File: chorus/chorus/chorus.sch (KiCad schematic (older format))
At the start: 39 parts

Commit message: working digital clock
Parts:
- removed C?: 220p, symbol Device:C
- removed C?: C, symbol Device:C
- removed R?: 3.8K, symbol Device:R
- removed RV?: 68K, symbol Device:R_POT
- added C? (x2): 10u, symbol Device:CP1
- added D? (x4): D, symbol Device:D
- added Q? (x2): 2N3906, Package_TO_SOT_THT:TO-92_Inline, symbol Transistor_BJT:2N3906
- added R? (x2): 2.8k, symbol Device:R
- added R?: 1K, symbol Device:R
- added R? (x2): 2.2k, symbol Device:R
- added R?: 10k, symbol Device:R
- added R?: 4.7k, symbol Device:R
- added RV?: 10K, symbol Device:R_POT
- added U? (x2): TL074, symbol Amplifier_Operational:TL074
- added U?: LM13700, symbol Amplifier_Operational:LM13700
- R?: value R -> 82K
- R?: value R -> 330K
- R?: value R -> 20K
- RV?: value R -> 500K
- U?: value MN3207 -> TL074
- U?: value MN3102 -> TL074
- U?: value ATtiny85-20PU -> TL074; footprint Package_DIP:DIP-8_W7.62mm -> (none)
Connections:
- net GND: now also U?.2 (-), U?.5 (+), D?.1 (K), D?.2 (A), Q?.1 (E), Q?.1 (E), R?.2, U?.12 (+); no longer U?.10 (+), U?.13 (-)
- net at R?.1: now also U?.7, C?.1, D?.1 (K), D?.2 (A); no longer U?.8
- net at RV?.3: now also U?.6 (-), C?.1; no longer U?.9 (-)
- net at R?.2, R?.2: now also U?.3 (+); no longer U?.12 (+)
- net at R?.1, R?.2: now also U?.1; no longer U?.14
- new net: C?.2, C?.2
- new net: D?.2 (A), D?.2 (A), R?.2
- new net: D?.1 (K), D?.1 (K), R?.2
- new net: R?.1, R?.2, U?.8
- new net: R?.1, R?.2, U?.9 (-)
- new net: R?.1, R?.1, U?.10 (+)
- new net: R?.1, RV?.1, RV?.2, U?.13 (-)
- new net: R?.1, RV?.3, U?.14
- new net: Q?.2 (B), Q?.2 (B), Q?.3 (C), R?.2
- new net: Q?.3 (C), R?.2
- new net: R?.1, U?.16
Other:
- note added: "depth ctrl"
- note added: "full wave rectifier"
- note added: "rate ctrl"
- note added: "triangle osc, 0.025Hz to 0.6Hz"
- note removed: "TODO: easier to drop the MN3102?\nCould use 555 or MCU\nJust needs low impedance opposite\nphase square waves 0-5V with switching\ntime < 500ns"
- moved on the sheet: R?, RV?

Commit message: calculated filters, updated parts
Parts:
- removed C?: 100n, symbol Device:C
- removed C?: C, symbol Device:C
- removed C? (x2): 10u, symbol Device:CP1
- removed D? (x4): D, symbol Device:D
- removed Q?: 2N3904, Package_TO_SOT_THT:TO-92_Inline, symbol Transistor_BJT:2N3904
- removed Q? (x2): 2N3906, Package_TO_SOT_THT:TO-92_Inline, symbol Transistor_BJT:2N3906
- removed R?: 100, symbol Device:R
- removed R? (x3): 100K, symbol Device:R
- removed R?: 82K, symbol Device:R
- removed R?: 330K, symbol Device:R
- removed R?: 20K, symbol Device:R
- removed R? (x2): 2.8k, symbol Device:R
- removed R?: 1K, symbol Device:R
- removed R? (x2): 2.2k, symbol Device:R
- removed R?: 10k, symbol Device:R
- removed R?: 4.7k, symbol Device:R
- removed RV?: 68K, symbol Device:R_POT
- removed RV?: 500K, symbol Device:R_POT
- removed RV?: 100K, symbol Device:R_POT
- removed RV?: 10K, symbol Device:R_POT
- removed U? (x5): TL074, symbol Amplifier_Operational:TL074
- removed U?: LM13700, symbol Amplifier_Operational:LM13700
- added C1, C2: 33n, Capacitor_THT:C_Disc_D6.0mm_W2.5mm_P5.00mm, symbol Device:C
- added D1, D2: LED, LED_THT:LED_D3.0mm, symbol Device:LED
- added J1: IN, Connector_Audio:Jack_6.35mm_Neutrik_NMJ6HCD2_Horizontal, symbol Connector:AudioJack3_Switch
- added J2: ISP, Connector_PinSocket_2.54mm:PinSocket_2x03_P2.54mm_Vertical, symbol Connector:AVR-ISP-6
- added J3: Jack-DC, Connector_PinSocket_2.54mm:PinSocket_2x01_P2.54mm_Vertical, symbol Connector:Jack-DC
- added J4: OUT, Connector_Audio:Jack_6.35mm_Neutrik_NMJ6HCD2_Horizontal, symbol Connector:AudioJack3_Switch
- added Q1: 2N3904, Package_TO_SOT_THT:TO-92_Inline, symbol Transistor_BJT:2N3904
- added R12, R13: 240, Resistor_THT:R_Axial_DIN0204_L3.6mm_D1.6mm_P2.54mm_Vertical, symbol Device:R
- added R3, R4: 1K, Resistor_THT:R_Axial_DIN0204_L3.6mm_D1.6mm_P2.54mm_Vertical, symbol Device:R
- added R5: 10K, Resistor_THT:R_Axial_DIN0204_L3.6mm_D1.6mm_P2.54mm_Vertical, symbol Device:R
- added R_CUTOFF_1: 100K, Potentiometer_THT:Potentiometer_Alps_RK09L_Double_Vertical, symbol Device:R_POT_Dual_Separate
- added SW1: SW_3PDT_x3, Button_Switch_THT:Stompbox Switch, symbol Switch:SW_3PDT_x3
- added unit 5 of U2
- added U5: LM7805, Package_TO_SOT_THT:TO-220-3_Vertical, symbol Regulator_Linear:LM7805_TO220
- added U6: TL072, Package_DIP:DIP-8_W7.62mm, symbol Amplifier_Operational:TL072
- C3: renamed from C?; footprint (none) -> Capacitor_THT:C_Disc_D6.0mm_W2.5mm_P5.00mm
- R1, R2: renamed from R?; value 100K -> 1M; footprint (none) -> Resistor_THT:R_Axial_DIN0204_L3.6mm_D1.6mm_P2.54mm_Vertical
- R10, R11, R8, R9: renamed from R?; footprint (none) -> Resistor_THT:R_Axial_DIN0204_L3.6mm_D1.6mm_P2.54mm_Vertical
- R6, R7: renamed from R?; value R -> 100K; footprint (none) -> Resistor_THT:R_Axial_DIN0204_L3.6mm_D1.6mm_P2.54mm_Vertical
- R_DEPTH1, R_RATE1: renamed from RV?; value 68K -> 100K; footprint (none) -> Potentiometer_THT:Potentiometer_Alps_RK09K_Single_Vertical
- R_FLANGE1: renamed from RV?; value 100K -> 1M; footprint (none) -> Potentiometer_THT:Potentiometer_Alps_RK09K_Single_Vertical
- U1: renamed from U?; value TL074 -> ATTINY85; footprint (none) -> Package_DIP:DIP-8_W7.62mm
- U2: renamed from U?; footprint (none) -> Package_DIP:DIP-14_W7.62mm
- U3: renamed from U?; value TL074 -> MN3102; footprint (none) -> Package_DIP:DIP-8_W7.62mm
- U4: renamed from U?; value TL074 -> MN3207; footprint (none) -> Package_DIP:DIP-8_W7.62mm
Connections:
- net +5V: now also R_DEPTH1.3, R_RATE1.3, U1.8 (VCC), D1.2 (A), D2.2 (A), J2.2 (VCC), U5.3 (VO)
- net +9V: now also R5.2, SW1.4 (A), U2.4 (V+), U5.1 (VI), U6.8 (V+)
- net GND: now also J2.6 (GND), J3.2, Q1.1 (E), R13.2, U2.11 (V-), U5.2 (GND), U6.4 (V-); no longer R8.1, R9.1, R_FLANGE1.3, U2.3 (+)
- net at R2.1, U2.1: now also C1.2; no longer U4.3 (IN)
- net BBD_CLOCK: now reaches U3.7 (OX1)
- net BBD_CLOCK: now also Q1.3 (C), R5.1
- net sheet629A6A5C/IN: now reaches R10.1, R11.1
- net at R1.1, R2.2, U2.2 (-): now also R_FLANGE1.3
- net at U2.5 (+): now also C2.1, R3.2
- net Anti-Aliasing Filter/IN: now reaches U2.6 (-), U2.7
- net Anti-Aliasing Filter/IN: now also R_CUTOFF_1.4; no longer R_FLANGE1.1
- net at R_FLANGE1.2: now also R_FLANGE1.1, U2.8, U2.9 (-); no longer U2.12 (+)
- net GNDA: now reaches U2.13 (-), U2.14
- net GNDA: now also R8.1, R9.1, U2.3 (+), J1.S, J1.SN, J1.TN, J4.S, J4.SN, J4.TN, R_CUTOFF_1.1
- net ~RST: now reaches U1.1 (~RESET~/PB5)
- net ~RST: now also J2.5 (~RST)
- net at U1.2 (XTAL1/PB3): now also R_RATE1.2
- net at U1.3 (XTAL2/PB4): now also R_DEPTH1.2
- net MOSI: now reaches U1.5 (AREF/PB0)
- net MOSI: now also J2.4 (MOSI), Q1.2 (B); no longer R_RATE1.2
- net LFO_CLOCK: now reaches U1.6 (PB1)
- net LFO_CLOCK: now also J2.1 (MISO), R12.2; no longer R_DEPTH1.2
- net SCK: now reaches U1.7 (PB2)
- net SCK: now also J2.3 (SCK)
- new net: R1.2, SW1.1 (A)
- new net: D1.1 (K), R12.1
- new net: D2.1 (K), R13.1
- new net: J3.1, SW1.5 (B)
- new net: R3.1, R_CUTOFF_1.2, R_CUTOFF_1.3
- new net: C1.1, C2.2, R4.2
- new net: R4.1, R_CUTOFF_1.5, R_CUTOFF_1.6
- new net: J1.R, J1.RN, J4.R, J4.RN
- new net: J1.T, SW1.2 (B)
- new net: J4.T, SW1.8 (B)
- new net: SW1.3 (C), SW1.9 (C)
- new net Anti-Aliasing Filter/OUT: U4.3 (IN)
- new net sheet629A6A5C/OUT: SW1.7 (A), U2.10 (+)
- no-connect marks 0 -> 3
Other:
- note added: "2nd order HPF, Q=0.5\nCutoff: 50Hz - 5KHz"
- note added: "BBD clock frequency is half the RC frequency\nDelay range: 2.54ms to 51.2ms (1024/f/2)"
- note added: "Clock input must be at least VDD-1V\nATTiny max is 6V\nTODO: are these levels correct?"
- note added: "ISP pins in case of firmware update"
- note added: "LFO indicator (optional)"
- note added: "NOTE: offically TL07x require higher minimum VCC\nthan 9V but I tested them and they seem to work fine"
- note added: "TODO: buffer here?"
- note added: "TODO: do we need an opamp for this?"
- note added: "TODO: do we need to scale down and back up the signal?"
- note added: "TODO: pots oriented correctly?"
- note added: "TODO: proper orientation?"
- note added: "input buffer / feedback sum\n1M input impedance"
- note added: "pwr indicator"
- note added: "uC generates LFO’d BBD clock in much less space than analog"
- note removed: "BBD clock frequency is half the RC frequency\nDelay range: 2.54ms to 51.2ms (1024/f/2)\n\nAlso need depth control"
- note removed: "HPF with variable tone"
- note removed: "depth ctrl"
- note removed: "flange amount"
- note removed: "full wave rectifier"
- note removed: "https://www.gadgetronicx.com/attiny85-timer-tutorial-generating-time-delay-interrupts/\nAlternatively to NPN, could just output on two pins"
- note removed: "rate ctrl"
- note removed: "triangle osc, 0.025Hz to 0.6Hz"
- note removed: "wet/dry\nTODO: some R combination that varies\nbetween 100% dry, 0% wet\nand 60% dry, 40% wet"
- moved on the sheet: C3, R1, R10, R11, R2, R6, R7, R8, R9, R_DEPTH1, R_FLANGE1, R_RATE1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

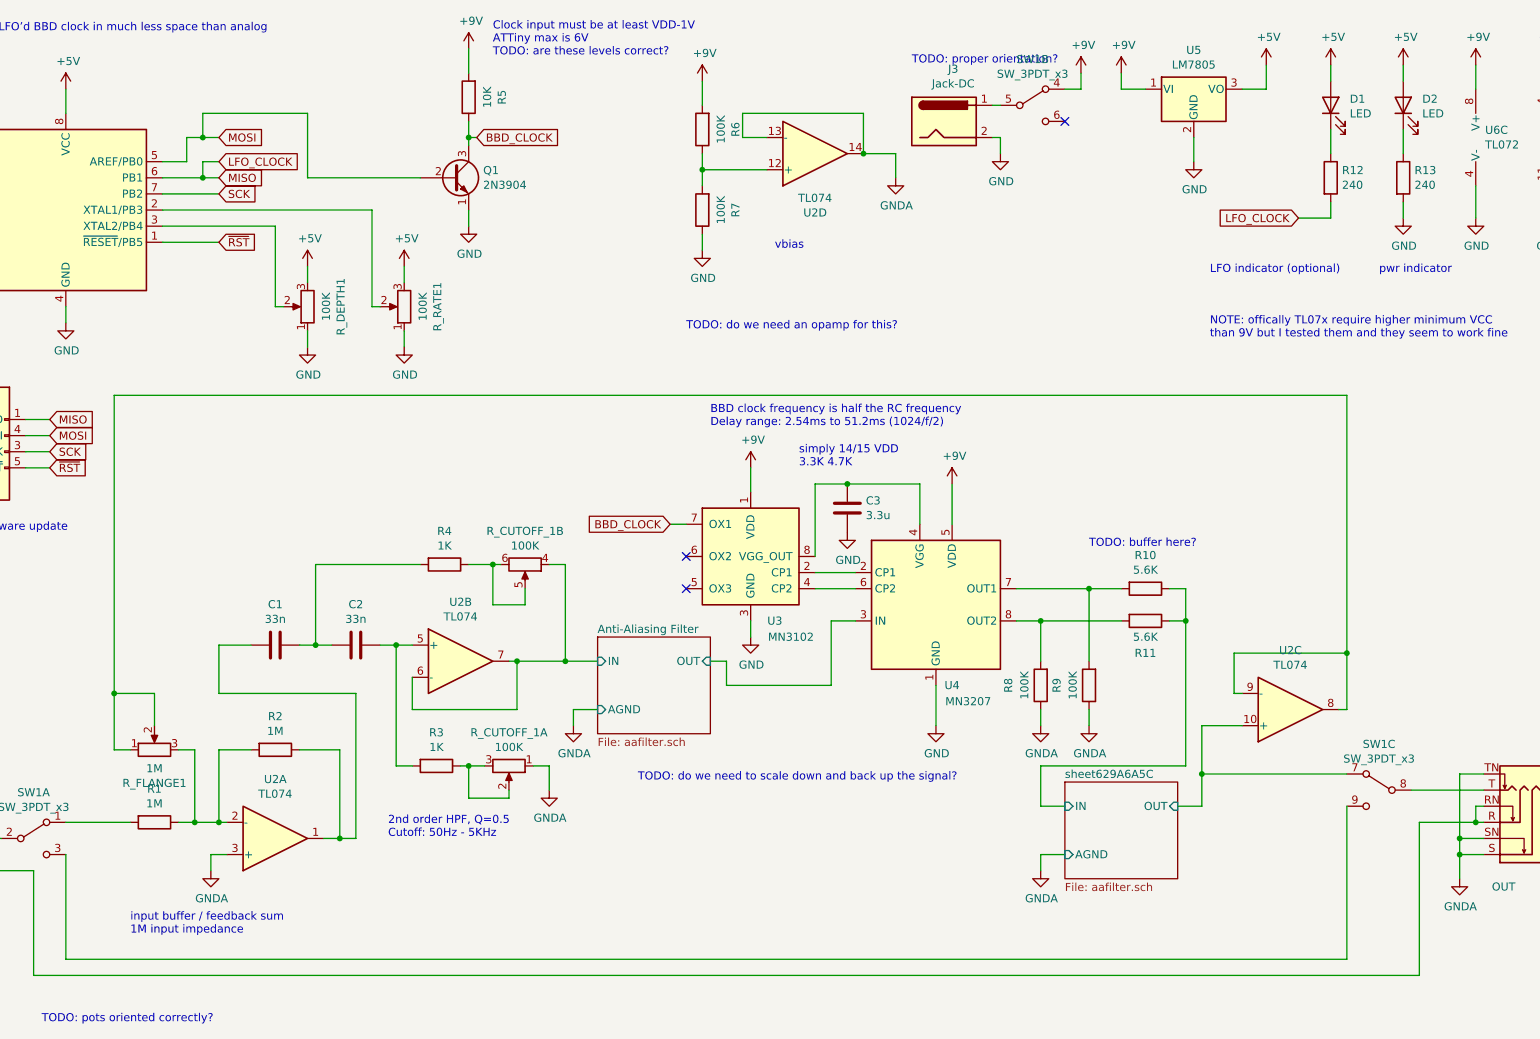
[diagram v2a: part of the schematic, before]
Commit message: learnings from breadboard, attiny resolution is too low
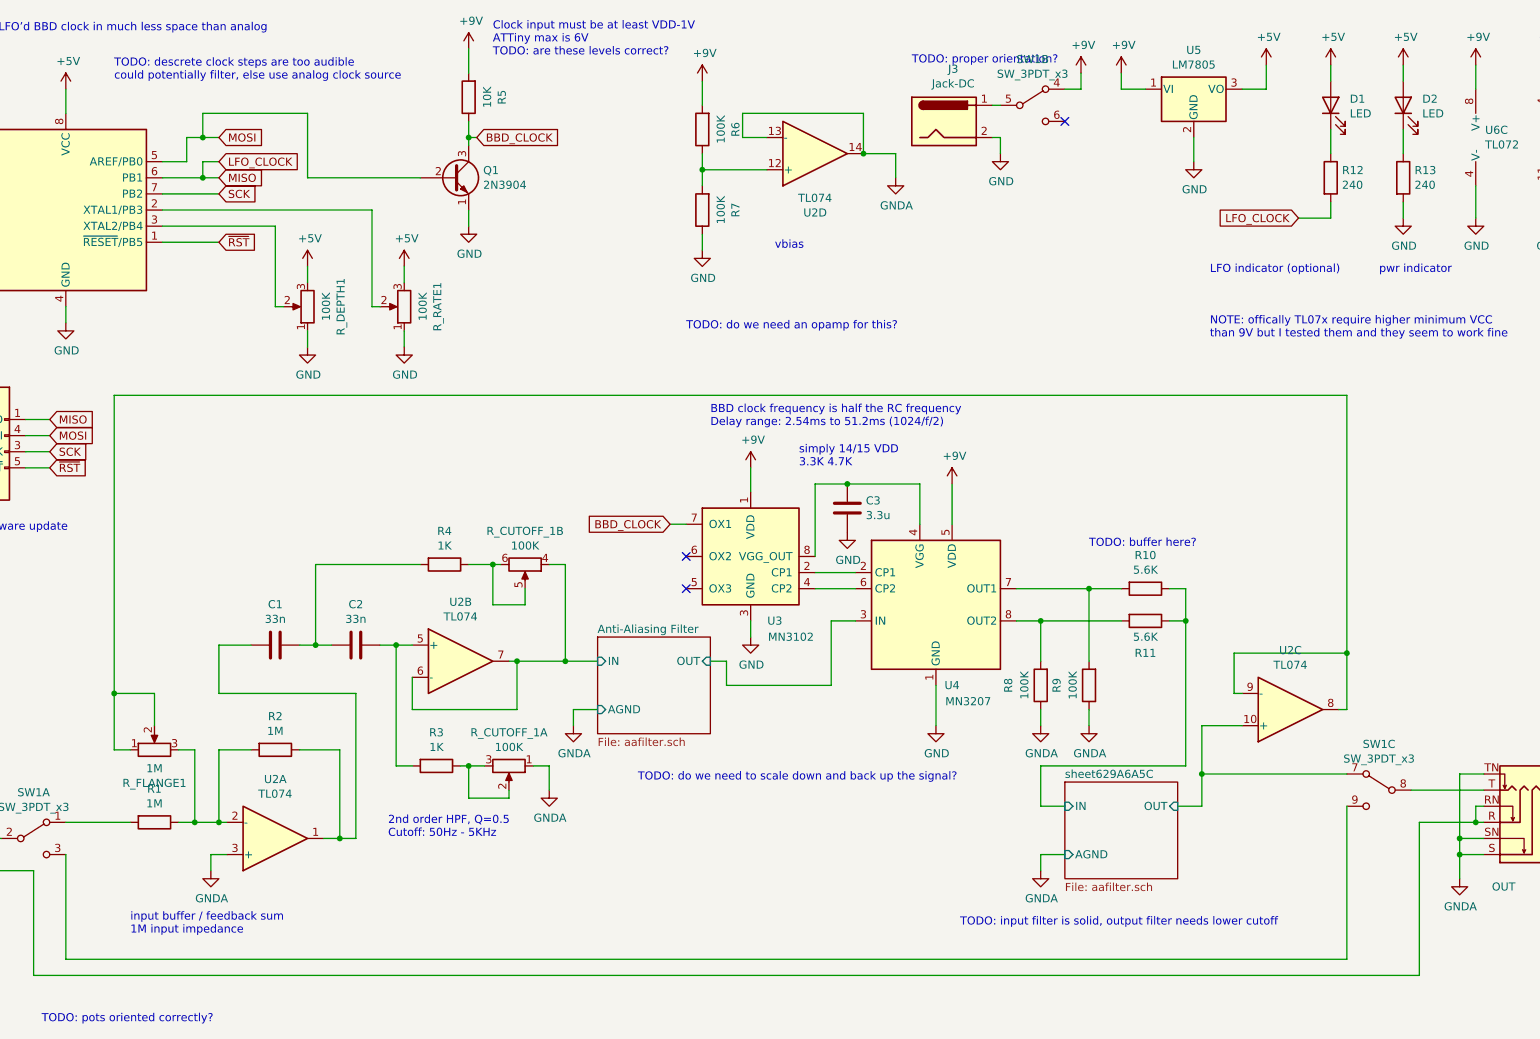
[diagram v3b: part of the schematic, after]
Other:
- note added: "TODO: descrete clock steps are too audible\ncould potentially filter, else use analog clock source"
- note added: "TODO: input filter is solid, output filter needs lower cutoff"
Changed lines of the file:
@@
 Wire Wire Line
 	8400 4250 7900 4250
-Connection ~ 8200 4050
-Wire Wire Line
-	8400 4050 8200 4050
-Wire Wire Line
-	8200 4050 8200 4500
-Wire Wire Line
-	7750 4050 8200 4050
 Wire Wire Line
 	7900 4250 7750 4250
@@
 Wire Wire Line
 	8200 4900 8200 4800
-$Comp
-L Device:R R9
-U 1 1 62451936
-P 8200 4650
-F 0 "R9" V 8400 4650 50  0000 C CNN
-F 1 "100K" V 8300 4650 50  0000 C CNN
-F 2 "Resistor_THT:R_Axial_DIN0204_L3.6mm_D1.6mm_P2.54mm_Vertical" V 8130 4650 50  0001 C CNN
-F 3 "~" H 8200 4650 50  0001 C CNN
-	1    8200 4650
-	-1   0    0    1
-$EndComp
 $Comp
 L Device:R R8
@@
 	1    0    0    -1
 $EndComp
+Text Notes 2150 900  0    50   ~ 0
+TODO: descrete clock steps are too audible\ncould potentially filter, else use analog clock source
+Text Notes 7400 6150 0    50   ~ 0
+TODO: input filter is solid, output filter needs lower cutoff
+$Comp
+L Device:R R9
+U 1 1 62451936
+P 8200 4650
+F 0 "R9" V 8400 4650 50  0000 C CNN
+F 1 "100K" V 8300 4650 50  0000 C CNN
+F 2 "Resistor_THT:R_Axial_DIN0204_L3.6mm_D1.6mm_P2.54mm_Vertical" V 8130 4650 50  0001 C CNN
+F 3 "~" H 8200 4650 50  0001 C CNN
+	1    8200 4650
+	-1   0    0    1
+$EndComp
+Wire Wire Line
+	7750 4050 8200 4050
+Wire Wire Line
+	8400 4050 8200 4050
+Connection ~ 8200 4050
+Wire Wire Line
+	8200 4050 8200 4500
 $EndSCHEMATC

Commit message: redesign
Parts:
- removed C1, C2: 33n, Capacitor_THT:C_Disc_D6.0mm_W2.5mm_P5.00mm, symbol Device:C
- removed C3: 3.3u, Capacitor_THT:C_Disc_D6.0mm_W2.5mm_P5.00mm, symbol Device:C
- removed D1: LED, LED_THT:LED_D3.0mm, symbol Device:LED
- removed J2: ISP, Connector_PinSocket_2.54mm:PinSocket_2x03_P2.54mm_Vertical, symbol Connector:AVR-ISP-6
- removed Q1: 2N3904, Package_TO_SOT_THT:TO-92_Inline, symbol Transistor_BJT:2N3904
- removed R10, R11: 5.6K, Resistor_THT:R_Axial_DIN0204_L3.6mm_D1.6mm_P2.54mm_Vertical, symbol Device:R
- removed R12: 240, Resistor_THT:R_Axial_DIN0204_L3.6mm_D1.6mm_P2.54mm_Vertical, symbol Device:R
- removed R3, R4: 1K, Resistor_THT:R_Axial_DIN0204_L3.6mm_D1.6mm_P2.54mm_Vertical, symbol Device:R
- removed R5: 10K, Resistor_THT:R_Axial_DIN0204_L3.6mm_D1.6mm_P2.54mm_Vertical, symbol Device:R
- removed R6, R7, R8, R9: 100K, Resistor_THT:R_Axial_DIN0204_L3.6mm_D1.6mm_P2.54mm_Vertical, symbol Device:R
- removed R_CUTOFF_1: 100K, Potentiometer_THT:Potentiometer_Alps_RK09L_Double_Vertical, symbol Device:R_POT_Dual_Separate
- removed R_DEPTH1, R_RATE1: 100K, Potentiometer_THT:Potentiometer_Alps_RK09K_Single_Vertical, symbol Device:R_POT
- removed U1: ATTINY85, Package_DIP:DIP-8_W7.62mm, symbol MCU_Microchip_ATtiny:ATtiny85-20PU
- removed unit 2 of U2
- removed unit 4 of U2
- removed unit 3 of U2
- removed U3: MN3102, Package_DIP:DIP-8_W7.62mm, symbol Timer:MN3102
- removed U4: MN3207, Package_DIP:DIP-8_W7.62mm, symbol Audio:MN3207
- added R? (x3): 1M, Resistor_THT:R_Axial_DIN0204_L3.6mm_D1.6mm_P2.54mm_Vertical, symbol Device:R
- added U8: TLE2426xLP, symbol Reference_Voltage:TLE2426xLP
- added U?: TL074, Package_DIP:DIP-14_W7.62mm, symbol Amplifier_Operational:TL074
- R13: value 240 -> 220
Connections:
- net +9V: now also U8.3 (IN)
- net GND: now also U8.2 (COMMON)
- net GNDA: now also U8.1 (OUT), U?.3 (+)
- net Tone Filter/IN: now reaches R2.1, U2.1
- net Anti-Aliasing Filter 2/OUT: now reaches R_FLANGE1.1, R_FLANGE1.2
- net Anti-Aliasing Filter 2/OUT: now also R?.2
- net at R1.2, SW1.1 (A): now also R?.2
- net sheet629A6A5C/OUT: no longer names the net of SW1.7 (A)
- net sheet629A6A5C/OUT: now also R?.1, U?.1
- new net: R?.1, R?.1, R?.2, U?.2 (-)
- no-connect marks 3 -> 1
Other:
- note added: "TODO: do we need to scale up and back down the signal\nto increase the dynamic range?"
- note added: "TODO: to reduce maximum feedback amount,\nadd additional resistance in series"
- note added: "TODO: wet/dry control?"
- note removed: "2nd order HPF, Q=0.5\nCutoff: 50Hz - 5KHz"
- note removed: "BBD clock frequency is half the RC frequency\nDelay range: 2.54ms to 51.2ms (1024/f/2)"
- note removed: "Clock input must be at least VDD-1V\nATTiny max is 6V\nTODO: are these levels correct?"
- note removed: "ISP pins in case of firmware update"
- note removed: "LFO indicator (optional)"
- note removed: "TODO: buffer here?"
- note removed: "TODO: descrete clock steps are too audible\ncould potentially filter, else use analog clock source"
- note removed: "TODO: do we need an opamp for this?"
- note removed: "TODO: do we need to scale down and back up the signal?"
- note removed: "simply 14/15 VDD\n3.3K 4.7K"
- note removed: "uC generates LFO’d BBD clock in much less space than analog"
- note removed: "vbias"
- moved on the sheet: D2, J1, J3, J4, R1, R13, R2, R_FLANGE1, SW1A, SW1B, SW1C, U2A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
